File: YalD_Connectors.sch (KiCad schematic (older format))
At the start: 22 parts, among them J1 RJDMXin, J2 RJDMXout, K2 DMXin, K3 DMXout, P1 PWR_IN, P10 CONN_01X04, P11 CONN_01X04, P12 CONN_01X04, P13 CONN_01X04, P14 CONN_01X02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

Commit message: fixed RJ45 connectors + folder libs.pretty added
RJ45 were on wrong side;
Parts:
- added P15, P16: CONN_01X01, Socket_Strips:Socket_Strip_Straight_1x01, symbol CONN_01X01
- P2: footprint Pin_Headers:Pin_Header_Straight_2x05 -> 2x5smd:Pin_HeadersPin_Header_SMD_2x5
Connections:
- wire segments 45 -> 34
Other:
- note added: "GND Bridge for unroutable path (sorry... please FIXME!)"
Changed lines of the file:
@@
 $EndDescr
 $Comp
-L GND #PWR021
+L GND #PWR022
 U 1 1 54499C10
 P 1300 1550
-F 0 "#PWR021" H 1300 1550 30  0001 C CNN
+F 0 "#PWR022" H 1300 1550 30  0001 C CNN
 F 1 "GND" H 1300 1480 30  0001 C CNN
 F 2 "" H 1300 1550 60  0001 C CNN
@@
 $EndComp
 $Comp
-L +12V #PWR022
+L +12V #PWR023
 U 1 1 54499C16
 P 1300 1200
-F 0 "#PWR022" H 1300 1150 20  0001 C CNN
+F 0 "#PWR023" H 1300 1150 20  0001 C CNN
 F 1 "+12V" H 1300 1300 30  0000 C CNN
 F 2 "" H 1300 1200 60  0001 C CNN
@@
 $EndComp
 $Comp
-L GND #PWR023
+L GND #PWR024
 U 1 1 54499C22
 P 1750 2850
-F 0 "#PWR023" H 1750 2850 30  0001 C CNN
+F 0 "#PWR024" H 1750 2850 30  0001 C CNN
 F 1 "GND" H 1750 2780 30  0001 C CNN
 F 2 "" H 1750 2850 60  0001 C CNN
@@
 $EndComp
 $Comp
-L VCC #PWR024
+L VCC #PWR025
 U 1 1 54499C28
 P 2400 2350
-F 0 "#PWR024" H 2400 2450 30  0001 C CNN
+F 0 "#PWR025" H 2400 2450 30  0001 C CNN
 F 1 "VCC" H 2400 2450 30  0000 C CNN
 F 2 "" H 2400 2350 60  0001 C CNN
@@
 $EndComp
 $Comp
-L +12V #PWR025
+L +12V #PWR026
 U 1 1 54499C2E
 P 1100 2350
-F 0 "#PWR025" H 1100 2300 20  0001 C CNN
+F 0 "#PWR026" H 1100 2300 20  0001 C CNN
 F 1 "+12V" H 1100 2450 30  0000 C CNN
 F 2 "" H 1100 2350 60  0001 C CNN
@@
 $EndComp
 $Comp
-L GND #PWR026
+L GND #PWR027
 U 1 1 54499C70
 P 2200 4350
-F 0 "#PWR026" H 2200 4350 30  0001 C CNN
+F 0 "#PWR027" H 2200 4350 30  0001 C CNN
 F 1 "GND" H 2200 4280 30  0001 C CNN
 F 2 "" H 2200 4350 60  0000 C CNN
@@
 DMXminus
 $Comp
-L VCC #PWR027
+L VCC #PWR028
 U 1 1 5449B31E
 P 4700 3550
-F 0 "#PWR027" H 4700 3650 30  0001 C CNN
+F 0 "#PWR028" H 4700 3650 30  0001 C CNN
 F 1 "VCC" H 4700 3650 30  0000 C CNN
 F 2 "" H 4700 3550 60  0001 C CNN
@@
 $EndComp
 $Comp
-L GND #PWR028
+L GND #PWR029
 U 1 1 5449B32A
 P 4700 4050
-F 0 "#PWR028" H 4700 4050 30  0001 C CNN
+F 0 "#PWR029" H 4700 4050 30  0001 C CNN
 F 1 "GND" H 4700 3980 30  0001 C CNN
 F 2 "" H 4700 4050 60  0001 C CNN
@@
 $EndComp
 $Comp
-L GND #PWR029
+L GND #PWR030
 U 1 1 5449E098
 P 4950 2200
-F 0 "#PWR029" H 4950 2200 30  0001 C CNN
+F 0 "#PWR030" H 4950 2200 30  0001 C CNN
 F 1 "GND" H 4950 2130 30  0001 C CNN
 F 2 "" H 4950 2200 60  0001 C CNN
@@
 $EndComp
 $Comp
-L VCC #PWR030
+L VCC #PWR031
 U 1 1 5449E09E
 P 4950 1650
-F 0 "#PWR030" H 4950 1750 30  0001 C CNN
+F 0 "#PWR031" H 4950 1750 30  0001 C CNN
 F 1 "VCC" H 4950 1750 30  0000 C CNN
 F 2 "" H 4950 1650 60  0001 C CNN
@@
 F 0 "P2" H 4450 2250 60  0000 C CNN
 F 1 "ISP" V 4450 1950 50  0000 C CNN
-F 2 "Pin_Headers:Pin_Header_Straight_2x05" H 4450 1950 60  0001 C CNN
+F 2 "2x5smd:Pin_HeadersPin_Header_SMD_2x5" H 4450 1950 60  0001 C CNN
 F 3 "" H 4450 1950 60  0001 C CNN
 	1    4450 1950
@@
 $EndComp
 $Comp
-L GND #PWR031
+L GND #PWR032
 U 1 1 544CF82B
 P 1200 2850
-F 0 "#PWR031" H 1200 2850 30  0001 C CNN
+F 0 "#PWR032" H 1200 2850 30  0001 C CNN
 F 1 "GND" H 1200 2780 30  0001 C CNN
 F 2 "" H 1200 2850 60  0001 C CNN
@@
 $EndComp
 $Comp
-L GND #PWR032
+L GND #PWR033
 U 1 1 544CF83E
 P 2300 2850
-F 0 "#PWR032" H 2300 2850 30  0001 C CNN
+F 0 "#PWR033" H 2300 2850 30  0001 C CNN
 F 1 "GND" H 2300 2780 30  0001 C CNN
 F 2 "" H 2300 2850 60  0001 C CNN
@@
 	1    0    0    -1
 $EndComp
-Connection ~ 1550 3850
-Wire Wire Line
-	1550 3850 1550 4450
-Wire Wire Line
-	1550 4450 1500 4450
-Connection ~ 1650 4200
-Wire Wire Line
-	1500 4550 1650 4550
-Wire Wire Line
-	1650 4550 1650 4200
-Wire Wire Line
-	1650 4200 1650 3950
-Wire Wire Line
-	2050 3750 1600 3750
-Wire Wire Line
-	1600 3750 1500 3750
-Wire Wire Line
-	1650 3950 1500 3950
-Wire Wire Line
-	2200 4200 1650 4200
-Wire Wire Line
-	1500 4350 1600 4350
-Wire Wire Line
-	1600 4350 1600 3750
-Connection ~ 1600 3750
-Wire Wire Line
-	2200 4350 2200 4200
-Wire Wire Line
-	1500 3850 1550 3850
-Wire Wire Line
-	1550 3850 2050 3850
-Wire Wire Line
-	4700 3950 4700 4050
-Connection ~ 4950 2150
-Wire Wire Line
-	4850 2150 4950 2150
-Connection ~ 4950 1950
-Wire Wire Line
-	4850 1950 4950 1950
-Wire Wire Line
-	4850 1850 4950 1850
-Wire Wire Line
-	4950 1850 4950 1950
-Wire Wire Line
-	4950 1950 4950 2050
-Wire Wire Line
-	4950 2050 4950 2150
-Wire Wire Line
-	4950 2150 4950 2200
-Wire Wire Line
-	4950 2050 4850 2050
-Connection ~ 4950 2050
-Wire Wire Line
-	4950 1650 4950 1750
-Wire Wire Line
-	4950 1750 4850 1750
-Wire Wire Line
-	2150 2350 2300 2350
-Wire Wire Line
-	2300 2350 2400 2350
-Wire Wire Line
-	1100 2350 1200 2350
-Wire Wire Line
-	1200 2350 1350 2350
-Wire Wire Line
-	1200 2450 1200 2350
-Connection ~ 1200 2350
-Wire Wire Line
-	2300 2450 2300 2350
-Connection ~ 2300 2350
-Wire Wire Line
-	1750 2650 1750 2850
-Wire Wire Line
-	1300 1200 1300 1300
-Wire Wire Line
-	1200 1300 1300 1300
-Wire Wire Line
-	1300 1300 1450 1300
-Wire Wire Line
-	1200 1500 1300 1500
-Wire Wire Line
-	1300 1500 1300 1550
-Connection ~ 1300 1300
 Text GLabel 1450 1300 2    60   Input ~ 0
 12V
@@
 	0    -1   -1   0
 $EndComp
-Text GLabel 1950 6900 2    51   Input ~ 0
+Text GLabel 1950 7000 2    51   Input ~ 0
+DMXplus
+Text GLabel 1950 5750 2    51   Input ~ 0
 DMXplus
 Text GLabel 1950 5650 2    51   Input ~ 0
-DMXplus
-Text GLabel 1950 5750 2    51   Input ~ 0
 DMXminus
-Text GLabel 1950 7000 2    51   Input ~ 0
+Text GLabel 1950 6900 2    51   Input ~ 0
 DMXminus
-Wire Wire Line
-	1950 6500 2600 6500
-Wire Wire Line
-	2600 6500 2600 6800
-Wire Wire Line
-	2600 6800 2600 6850
-Wire Wire Line
-	2600 6800 1950 6800
-Connection ~ 2600 6800
-Wire Wire Line
-	1950 5250 2600 5250
-Wire Wire Line
-	2600 5250 2600 5550
-Wire Wire Line
-	2600 5550 2600 5600
-Wire Wire Line
-	2600 5550 1950 5550
-Connection ~ 2600 5550
-$Comp
-L GND #PWR033
+$Comp
+L GND #PWR034
 U 1 1 54500FB5
 P 2600 5600
-F 0 "#PWR033" H 2600 5600 30  0001 C CNN
+F 0 "#PWR034" H 2600 5600 30  0001 C CNN
 F 1 "GND" H 2600 5530 30  0001 C CNN
 F 2 "" H 2600 5600 60  0000 C CNN
@@
 $EndComp
 $Comp
-L GND #PWR034
+L GND #PWR035
 U 1 1 54500FD5
 P 2600 6850
-F 0 "#PWR034" H 2600 6850 30  0001 C CNN
+F 0 "#PWR035" H 2600 6850 30  0001 C CNN
 F 1 "GND" H 2600 6780 30  0001 C CNN
 F 2 "" H 2600 6850 60  0000 C CNN
@@
 	1    0    0    -1
 $EndComp
+$Comp
+L CONN_01X01 P15
+U 1 1 544EE0CC
+P 5200 5300
+F 0 "P15" H 5200 5400 50  0000 C CNN
+F 1 "CONN_01X01" V 5300 5300 50  0000 C CNN
+F 2 "Socket_Strips:Socket_Strip_Straight_1x01" H 5200 5300 60  0001 C CNN
+F 3 "" H 5200 5300 60  0000 C CNN
+	1    5200 5300
+	0    -1   -1   0
+$EndComp
+$Comp
+L CONN_01X01 P16
+U 1 1 544EE148
+P 6050 5300
+F 0 "P16" H 6050 5400 50  0000 C CNN
+F 1 "CONN_01X01" V 6150 5300 50  0000 C CNN
+F 2 "Socket_Strips:Socket_Strip_Straight_1x01" H 6050 5300 60  0001 C CNN
+F 3 "" H 6050 5300 60  0000 C CNN
+	1    6050 5300
+	0    -1   -1   0
+$EndComp
+$Comp
+L GND #PWR036
+U 1 1 544EE424
+P 5200 5500
+F 0 "#PWR036" H 5200 5500 30  0001 C CNN
+F 1 "GND" H 5200 5430 30  0001 C CNN
+F 2 "" H 5200 5500 60  0000 C CNN
+F 3 "" H 5200 5500 60  0000 C CNN
+	1    5200 5500
+	1    0    0    -1
+$EndComp
+$Comp
+L GND #PWR037
+U 1 1 544EE44E
+P 6050 5500
+F 0 "#PWR037" H 6050 5500 30  0001 C CNN
+F 1 "GND" H 6050 5430 30  0001 C CNN
+F 2 "" H 6050 5500 60  0000 C CNN
+F 3 "" H 6050 5500 60  0000 C CNN
+	1    6050 5500
+	1    0    0    -1
+$EndComp
+Text Notes 4400 5000 0    60   ~ 0
+GND Bridge for unroutable path (sorry... please FIXME!)
+Connection ~ 1550 3850
+Wire Wire Line
+	1550 3850 1550 4450
+Wire Wire Line
+	1550 4450 1500 4450
+Connection ~ 1650 4200
+Wire Wire Line
+	1650 4550 1500 4550
+Wire Wire Line
+	1650 3950 1650 4550
+Wire Wire Line
+	1500 3750 2050 3750
+Wire Wire Line
+	1650 3950 1500 3950
+Wire Wire Line
+	2200 4200 1650 4200
+Wire Wire Line
+	1500 4350 1600 4350
+Wire Wire Line
+	1600 4350 1600 3750
+Connection ~ 1600 3750
+Wire Wire Line
+	2200 4350 2200 4200
+Wire Wire Line
+	1500 3850 2050 3850
+Wire Wire Line
+	4700 3950 4700 4050
+Connection ~ 4950 2150
+Wire Wire Line
+	4950 2150 4850 2150
+Connection ~ 4950 1950
+Wire Wire Line
+	4850 1950 4950 1950
+Wire Wire Line
+	4850 1850 4950 1850
+Wire Wire Line
+	4950 1850 4950 2200
+Wire Wire Line
+	4950 2050 4850 2050
+Connection ~ 4950 2050
+Wire Wire Line
+	4950 1650 4950 1750
+Wire Wire Line
+	4950 1750 4850 1750
+Wire Wire Line
+	2150 2350 2400 2350
+Wire Wire Line
+	1100 2350 1350 2350
+Wire Wire Line
+	1200 2450 1200 2350
+Connection ~ 1200 2350
+Wire Wire Line
+	2300 2450 2300 2350
+Connection ~ 2300 2350
+Wire Wire Line
+	1750 2650 1750 2850
+Wire Wire Line
+	1300 1200 1300 1300
+Wire Wire Line
+	1200 1300 1450 1300
+Wire Wire Line
+	1200 1500 1300 1500
+Wire Wire Line
+	1300 1500 1300 1550
+Connection ~ 1300 1300
+Wire Wire Line
+	2600 6300 2600 6850
+Wire Wire Line
+	2600 5050 2600 5600
+Wire Wire Line
+	1950 5050 2600 5050
+Wire Wire Line
+	1950 6300 2600 6300
+Wire Wire Line
+	1950 6400 2600 6400
+Connection ~ 2600 6400
+Wire Wire Line
+	1950 5150 2600 5150
+Connection ~ 2600 5150
 $EndSCHEMATC

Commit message: DMX plus/minus switched, GND airwire connected
+ nicer silk print (more readable)
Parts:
- removed P15, P16: CONN_01X01, Socket_Strips:Socket_Strip_Straight_1x01, symbol CONN_01X01
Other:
- note removed: "GND Bridge for unroutable path (sorry... please FIXME!)"
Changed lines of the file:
@@
 $EndComp
 Text GLabel 2050 3750 2    51   Input ~ 0
+DMXminus
+Text GLabel 2050 3850 2    51   Input ~ 0
 DMXplus
-Text GLabel 2050 3850 2    51   Input ~ 0
-DMXminus
 $Comp
 L VCC #PWR028
@@
 	1    0    0    -1
 $EndComp
-$Comp
-L CONN_01X01 P15
-U 1 1 544EE0CC
-P 5200 5300
-F 0 "P15" H 5200 5400 50  0000 C CNN
-F 1 "CONN_01X01" V 5300 5300 50  0000 C CNN
-F 2 "Socket_Strips:Socket_Strip_Straight_1x01" H 5200 5300 60  0001 C CNN
-F 3 "" H 5200 5300 60  0000 C CNN
-	1    5200 5300
-	0    -1   -1   0
-$EndComp
-$Comp
-L CONN_01X01 P16
-U 1 1 544EE148
-P 6050 5300
-F 0 "P16" H 6050 5400 50  0000 C CNN
-F 1 "CONN_01X01" V 6150 5300 50  0000 C CNN
-F 2 "Socket_Strips:Socket_Strip_Straight_1x01" H 6050 5300 60  0001 C CNN
-F 3 "" H 6050 5300 60  0000 C CNN
-	1    6050 5300
-	0    -1   -1   0
-$EndComp
-$Comp
-L GND #PWR036
-U 1 1 544EE424
-P 5200 5500
-F 0 "#PWR036" H 5200 5500 30  0001 C CNN
-F 1 "GND" H 5200 5430 30  0001 C CNN
-F 2 "" H 5200 5500 60  0000 C CNN
-F 3 "" H 5200 5500 60  0000 C CNN
-	1    5200 5500
-	1    0    0    -1
-$EndComp
-$Comp
-L GND #PWR037
-U 1 1 544EE44E
-P 6050 5500
-F 0 "#PWR037" H 6050 5500 30  0001 C CNN
-F 1 "GND" H 6050 5430 30  0001 C CNN
-F 2 "" H 6050 5500 60  0000 C CNN
-F 3 "" H 6050 5500 60  0000 C CNN
-	1    6050 5500
-	1    0    0    -1
-$EndComp
-Text Notes 4400 5000 0    60   ~ 0
-GND Bridge for unroutable path (sorry... please FIXME!)
 Connection ~ 1550 3850
 Wire Wire Line

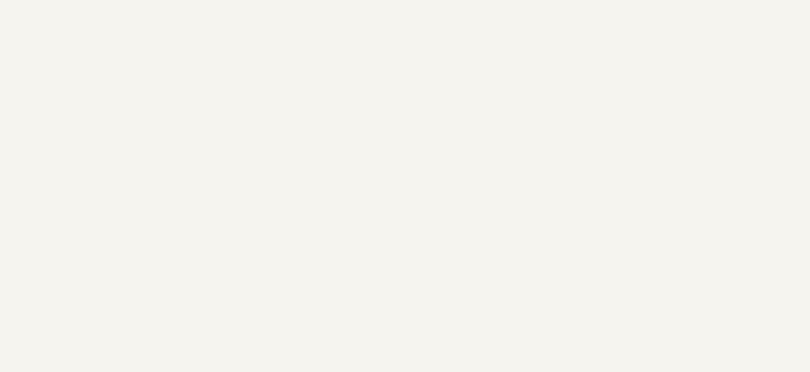
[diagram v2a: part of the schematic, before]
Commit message: added debug connector (software UART TX)
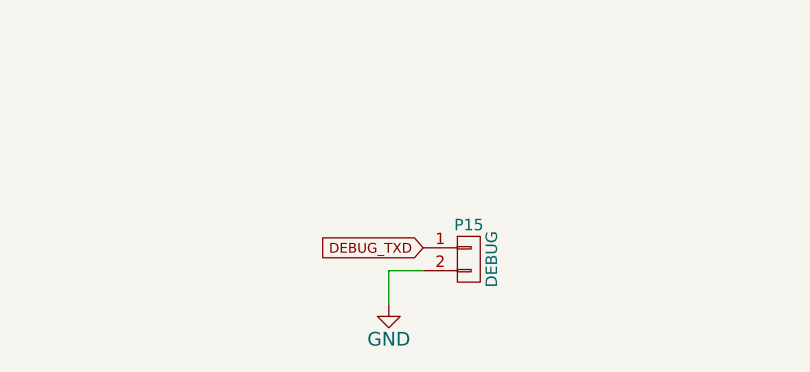
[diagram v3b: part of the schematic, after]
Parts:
- added P15: DEBUG, Pin_Headers:Pin_Header_Straight_1x02, symbol CONN_01X02
- P2: footprint 2x5smd:Pin_HeadersPin_Header_SMD_2x5 -> Pin_Headers:Pin_Header_Straight_2x05
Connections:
- net GND: now also P15.2 (P2)
- new net DEBUG_TXD: P15.1 (P1)
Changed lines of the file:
@@
 LIBS:contrib
 LIBS:valves
-LIBS:pca9685
-LIBS:dips-s
-LIBS:irf-2
-LIBS:conn_17x2
 LIBS:7805_f
 LIBS:YaLD-cache
@@
 F 0 "P2" H 4450 2250 60  0000 C CNN
 F 1 "ISP" V 4450 1950 50  0000 C CNN
-F 2 "2x5smd:Pin_HeadersPin_Header_SMD_2x5" H 4450 1950 60  0001 C CNN
+F 2 "Pin_Headers:Pin_Header_Straight_2x05" H 4450 1950 60  0001 C CNN
 F 3 "" H 4450 1950 60  0001 C CNN
 	1    4450 1950
@@
 	1950 5150 2600 5150
 Connection ~ 2600 5150
+$Comp
+L CONN_01X02 P15
+U 1 1 54D1467D
+P 6150 6900
+F 0 "P15" H 6150 7050 50  0000 C CNN
+F 1 "DEBUG" V 6250 6900 50  0000 C CNN
+F 2 "Pin_Headers:Pin_Header_Straight_1x02" H 6150 6900 60  0001 C CNN
+F 3 "" H 6150 6900 60  0000 C CNN
+	1    6150 6900
+	1    0    0    -1
+$EndComp
+Wire Wire Line
+	5950 6950 5800 6950
+Wire Wire Line
+	5800 6950 5800 7100
+$Comp
+L GND #PWR036
+U 1 1 54D155A2
+P 5800 7100
+F 0 "#PWR036" H 5800 6850 60  0001 C CNN
+F 1 "GND" H 5800 6950 60  0000 C CNN
+F 2 "" H 5800 7100 60  0000 C CNN
+F 3 "" H 5800 7100 60  0000 C CNN
+	1    5800 7100
+	1    0    0    -1
+$EndComp
+Text GLabel 5950 6850 0    43   Input ~ 0
+DEBUG_TXD
 $EndSCHEMATC

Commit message: changed outputs to 3.5mm pitch
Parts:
- removed P14, P3: CONN_01X02, Pin_Headers:Pin_Header_Straight_1x02, symbol CONN_01X02
- added P16: UART, Pin_Headers:Pin_Header_Straight_1x04, symbol CONN_01X04
- added P3: CONN_01X04, CONN_1_4_Pitch_3_5:CONN_1_4_XY350_Pitch_3.5, symbol CONN_01X04
- C4, C5, C6: symbol C -> C-RESCUE-YaLD
- P10, P11, P12, P13, P4, P5, P6, P7, P8, P9: footprint Pin_Headers:Pin_Header_Straight_1x04 -> CONN_1_4_Pitch_3_5:CONN_1_4_XY350_Pitch_3.5
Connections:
- net +12V: now also P3.1 (P1), P3.3 (P3)
- net GND: now also P16.1 (P1)
- net OUT0: now also P3.2 (P2)
- net OUT15: now also P3.4 (P4)
- net VCC: now also P16.2 (P2)
- new net RXD: P16.4 (P4)
- new net TXD: P16.3 (P3)
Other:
- moved on the sheet: C5
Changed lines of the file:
@@
 EESchema Schematic File Version 2
+LIBS:YaLD-rescue
 LIBS:power
 LIBS:device
@@
 LIBS:memory
 LIBS:xilinx
-LIBS:special
 LIBS:microcontrollers
 LIBS:dsp
@@
 L VCC #PWR028
 U 1 1 5449B31E
-P 4700 3550
-F 0 "#PWR028" H 4700 3650 30  0001 C CNN
-F 1 "VCC" H 4700 3650 30  0000 C CNN
-F 2 "" H 4700 3550 60  0001 C CNN
-F 3 "" H 4700 3550 60  0001 C CNN
-	1    4700 3550
-	1    0    0    -1
-$EndComp
-$Comp
-L C C5
+P 5900 3550
+F 0 "#PWR028" H 5900 3650 30  0001 C CNN
+F 1 "VCC" H 5900 3650 30  0000 C CNN
+F 2 "" H 5900 3550 60  0001 C CNN
+F 3 "" H 5900 3550 60  0001 C CNN
+	1    5900 3550
+	1    0    0    -1
+$EndComp
+$Comp
+L C-RESCUE-YaLD C5
 U 1 1 5449B324
-P 4700 3750
-F 0 "C5" H 4750 3850 50  0000 L CNN
-F 1 "100n" H 4750 3650 50  0000 L CNN
-F 2 "SMD_Packages:SMD-0805" H 4700 3750 60  0001 C CNN
-F 3 "" H 4700 3750 60  0001 C CNN
-	1    4700 3750
+P 5900 3750
+AR Path="/5449B324" Ref="C5"  Part="1"
+AR Path="/54499BE5/5449B324" Ref="C5"  Part="1"
+F 0 "C5" H 5950 3850 50  0000 L CNN
+F 1 "100n" H 5950 3650 50  0000 L CNN
+F 2 "SMD_Packages:SMD-0805" H 5900 3750 60  0001 C CNN
+F 3 "" H 5900 3750 60  0001 C CNN
+	1    5900 3750
 	1    0    0    -1
 $EndComp
@@
 L GND #PWR029
 U 1 1 5449B32A
-P 4700 4050
-F 0 "#PWR029" H 4700 4050 30  0001 C CNN
-F 1 "GND" H 4700 3980 30  0001 C CNN
-F 2 "" H 4700 4050 60  0001 C CNN
-F 3 "" H 4700 4050 60  0001 C CNN
-	1    4700 4050
+P 5900 4050
+F 0 "#PWR029" H 5900 4050 30  0001 C CNN
+F 1 "GND" H 5900 3980 30  0001 C CNN
+F 2 "" H 5900 4050 60  0001 C CNN
+F 3 "" H 5900 4050 60  0001 C CNN
+	1    5900 4050
 	1    0    0    -1
 $EndComp
@@
 SCK
 $Comp
-L C C4
+L C-RESCUE-YaLD C4
 U 1 1 544CF707
 P 1200 2650
+AR Path="/544CF707" Ref="C4"  Part="1"
+AR Path="/54499BE5/544CF707" Ref="C4"  Part="1"
 F 0 "C4" H 1200 2750 40  0000 L CNN
 F 1 "330n" H 1206 2565 40  0000 L CNN
@@
 $EndComp
 $Comp
-L C C6
+L C-RESCUE-YaLD C6
 U 1 1 544CF785
 P 2300 2650
+AR Path="/544CF785" Ref="C6"  Part="1"
+AR Path="/54499BE5/544CF785" Ref="C6"  Part="1"
 F 0 "C6" H 2300 2750 40  0000 L CNN
 F 1 "100n" H 2306 2565 40  0000 L CNN
@@
 Text GLabel 1450 1300 2    60   Input ~ 0
 12V
-Text GLabel 9700 3950 0    47   Input ~ 0
-12V
-Text GLabel 9700 4050 0    47   Input ~ 0
+Text GLabel 9700 5850 0    47   Input ~ 0
+12V
+Text GLabel 9700 5950 0    47   Input ~ 0
 OUT0
 Text GLabel 10650 1000 0    47   Input ~ 0
@@
 F 0 "P4" H 10850 1300 50  0000 C CNN
 F 1 "CONN_01X04" V 10950 1050 50  0000 C CNN
-F 2 "Pin_Headers:Pin_Header_Straight_1x04" H 10850 1050 60  0001 C CNN
+F 2 "CONN_1_4_Pitch_3_5:CONN_1_4_XY350_Pitch_3.5" H 10850 1050 60  0001 C CNN
 F 3 "" H 10850 1050 60  0000 C CNN
 	1    10850 1050
@@
 F 0 "P5" H 10850 1850 50  0000 C CNN
 F 1 "CONN_01X04" V 10950 1600 50  0000 C CNN
-F 2 "Pin_Headers:Pin_Header_Straight_1x04" H 10850 1600 60  0001 C CNN
+F 2 "CONN_1_4_Pitch_3_5:CONN_1_4_XY350_Pitch_3.5" H 10850 1600 60  0001 C CNN
 F 3 "" H 10850 1600 60  0000 C CNN
 	1    10850 1600
@@
 F 0 "P6" H 10850 2400 50  0000 C CNN
 F 1 "CONN_01X04" V 10950 2150 50  0000 C CNN
-F 2 "Pin_Headers:Pin_Header_Straight_1x04" H 10850 2150 60  0001 C CNN
+F 2 "CONN_1_4_Pitch_3_5:CONN_1_4_XY350_Pitch_3.5" H 10850 2150 60  0001 C CNN
 F 3 "" H 10850 2150 60  0000 C CNN
 	1    10850 2150
@@
 F 0 "P7" H 10850 2950 50  0000 C CNN
 F 1 "CONN_01X04" V 10950 2700 50  0000 C CNN
-F 2 "Pin_Headers:Pin_Header_Straight_1x04" H 10850 2700 60  0001 C CNN
+F 2 "CONN_1_4_Pitch_3_5:CONN_1_4_XY350_Pitch_3.5" H 10850 2700 60  0001 C CNN
 F 3 "" H 10850 2700 60  0000 C CNN
 	1    10850 2700
@@
 F 0 "P8" H 10850 3500 50  0000 C CNN
 F 1 "CONN_01X04" V 10950 3250 50  0000 C CNN
-F 2 "Pin_Headers:Pin_Header_Straight_1x04" H 10850 3250 60  0001 C CNN
+F 2 "CONN_1_4_Pitch_3_5:CONN_1_4_XY350_Pitch_3.5" H 10850 3250 60  0001 C CNN
 F 3 "" H 10850 3250 60  0000 C CNN
 	1    10850 3250
@@
 Text GLabel 10650 3100 0    47   Input ~ 0
 12V
-Text GLabel 9700 4750 0    47   Input ~ 0
+Text GLabel 9700 6150 0    47   Input ~ 0
 OUT15
 Text GLabel 10650 3300 0    47   Input ~ 0
@@
 F 0 "P9" H 10850 4050 50  0000 C CNN
 F 1 "CONN_01X04" V 10950 3800 50  0000 C CNN
-F 2 "Pin_Headers:Pin_Header_Straight_1x04" H 10850 3800 60  0001 C CNN
+F 2 "CONN_1_4_Pitch_3_5:CONN_1_4_XY350_Pitch_3.5" H 10850 3800 60  0001 C CNN
 F 3 "" H 10850 3800 60  0000 C CNN
 	1    10850 3800
@@
 F 0 "P10" H 10850 4600 50  0000 C CNN
 F 1 "CONN_01X04" V 10950 4350 50  0000 C CNN
-F 2 "Pin_Headers:Pin_Header_Straight_1x04" H 10850 4350 60  0001 C CNN
+F 2 "CONN_1_4_Pitch_3_5:CONN_1_4_XY350_Pitch_3.5" H 10850 4350 60  0001 C CNN
 F 3 "" H 10850 4350 60  0000 C CNN
 	1    10850 4350
@@
 F 0 "P11" H 10850 5150 50  0000 C CNN
 F 1 "CONN_01X04" V 10950 4900 50  0000 C CNN
-F 2 "Pin_Headers:Pin_Header_Straight_1x04" H 10850 4900 60  0001 C CNN
+F 2 "CONN_1_4_Pitch_3_5:CONN_1_4_XY350_Pitch_3.5" H 10850 4900 60  0001 C CNN
 F 3 "" H 10850 4900 60  0000 C CNN
 	1    10850 4900
@@
 F 0 "P12" H 10850 5700 50  0000 C CNN
 F 1 "CONN_01X04" V 10950 5450 50  0000 C CNN
-F 2 "Pin_Headers:Pin_Header_Straight_1x04" H 10850 5450 60  0001 C CNN
+F 2 "CONN_1_4_Pitch_3_5:CONN_1_4_XY350_Pitch_3.5" H 10850 5450 60  0001 C CNN
 F 3 "" H 10850 5450 60  0000 C CNN
 	1    10850 5450
@@
 F 0 "P13" H 10850 6250 50  0000 C CNN
 F 1 "CONN_01X04" V 10950 6000 50  0000 C CNN
-F 2 "Pin_Headers:Pin_Header_Straight_1x04" H 10850 6000 60  0001 C CNN
+F 2 "CONN_1_4_Pitch_3_5:CONN_1_4_XY350_Pitch_3.5" H 10850 6000 60  0001 C CNN
 F 3 "" H 10850 6000 60  0000 C CNN
 	1    10850 6000
@@
 Text GLabel 10650 6050 0    47   Input ~ 0
 OUT31
-Text GLabel 9700 4650 0    47   Input ~ 0
+Text GLabel 9700 6050 0    47   Input ~ 0
 12V
 NoConn ~ 4050 1850
@@
 	1    0    0    -1
 $EndComp
-$Comp
-L CONN_01X02 P3
-U 1 1 544D5126
-P 9900 4000
-F 0 "P3" H 9900 4150 50  0000 C CNN
-F 1 "CONN_01X02" V 10000 4000 50  0000 C CNN
-F 2 "Pin_Headers:Pin_Header_Straight_1x02" H 9900 4000 60  0001 C CNN
-F 3 "" H 9900 4000 60  0000 C CNN
-	1    9900 4000
-	1    0    0    -1
-$EndComp
-$Comp
-L CONN_01X02 P14
-U 1 1 544D520E
-P 9900 4700
-F 0 "P14" H 9900 4850 50  0000 C CNN
-F 1 "CONN_01X02" V 10000 4700 50  0000 C CNN
-F 2 "Pin_Headers:Pin_Header_Straight_1x02" H 9900 4700 60  0001 C CNN
-F 3 "" H 9900 4700 60  0000 C CNN
-	1    9900 4700
-	1    0    0    -1
-$EndComp
 Connection ~ 1550 3850
 Wire Wire Line
@@
 	1500 3850 2050 3850
 Wire Wire Line
-	4700 3950 4700 4050
+	5900 3950 5900 4050
 Connection ~ 4950 2150
 Wire Wire Line
@@
 Text GLabel 5950 6850 0    43   Input ~ 0
 DEBUG_TXD
+$Comp
+L CONN_01X04 P16
+U 1 1 57BF2A8E
+P 3350 4100
+F 0 "P16" H 3269 3725 50  0000 C CNN
+F 1 "UART" H 3269 3816 50  0000 C CNN
+F 2 "Pin_Headers:Pin_Header_Straight_1x04" H 3350 4100 50  0001 C CNN
+F 3 "" H 3350 4100 50  0000 C CNN
+	1    3350 4100
+	-1   0    0    1
+$EndComp
+Text GLabel 3550 3950 2    60   Input ~ 0
+RXD
+Text GLabel 3550 4050 2    60   Input ~ 0
+TXD
+$Comp
+L VCC #PWR037
+U 1 1 57BF4820
+P 4000 3550
+F 0 "#PWR037" H 4000 3650 30  0001 C CNN
+F 1 "VCC" H 4000 3650 30  0000 C CNN
+F 2 "" H 4000 3550 60  0001 C CNN
+F 3 "" H 4000 3550 60  0001 C CNN
+	1    4000 3550
+	1    0    0    -1
+$EndComp
+$Comp
+L GND #PWR038
+U 1 1 57BF4F4B
+P 4000 4350
+F 0 "#PWR038" H 4000 4350 30  0001 C CNN
+F 1 "GND" H 4000 4280 30  0001 C CNN
+F 2 "" H 4000 4350 60  0000 C CNN
+F 3 "" H 4000 4350 60  0000 C CNN
+	1    4000 4350
+	1    0    0    -1
+$EndComp
+Wire Wire Line
+	3550 4250 4000 4250
+Wire Wire Line
+	4000 4250 4000 4350
+Wire Wire Line
+	3550 4150 4000 4150
+Wire Wire Line
+	4000 4150 4000 3550
+$Comp
+L CONN_01X04 P3
+U 1 1 57BF799B
+P 9900 6000
+F 0 "P3" H 9900 6250 50  0000 C CNN
+F 1 "CONN_01X04" V 10000 6000 50  0000 C CNN
+F 2 "CONN_1_4_Pitch_3_5:CONN_1_4_XY350_Pitch_3.5" H 9900 6000 60  0001 C CNN
+F 3 "" H 9900 6000 60  0000 C CNN
+	1    9900 6000
+	1    0    0    -1
+$EndComp
 $EndSCHEMATC
